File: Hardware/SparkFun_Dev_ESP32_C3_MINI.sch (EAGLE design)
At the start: 40 parts, among them J1 USB Female Type C Connector, J5 Vertical Qwiic Connector, U1 ESP32-C3_MINI-1, U2 RT9080-33GJ5

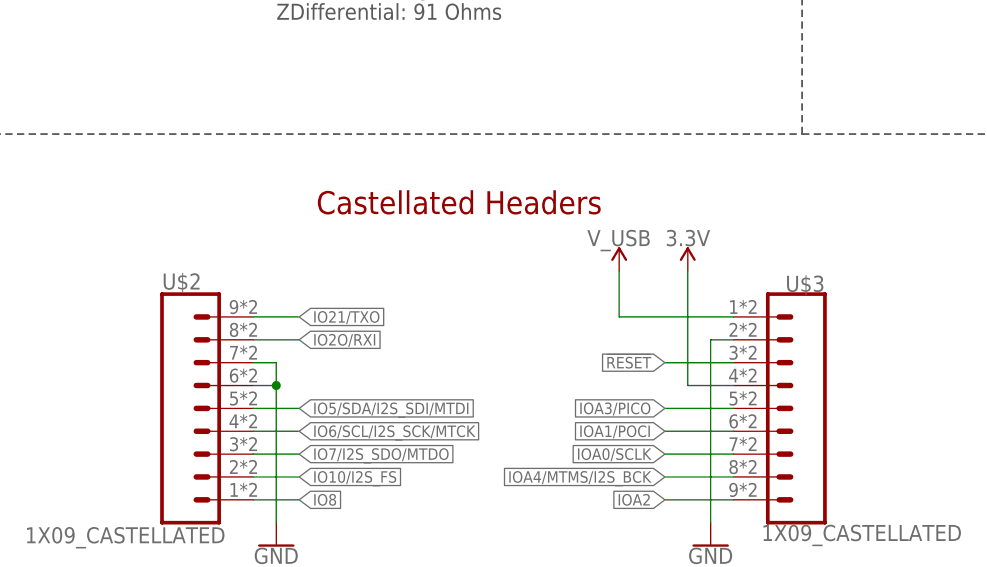
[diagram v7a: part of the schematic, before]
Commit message: Adds SparkFun logo
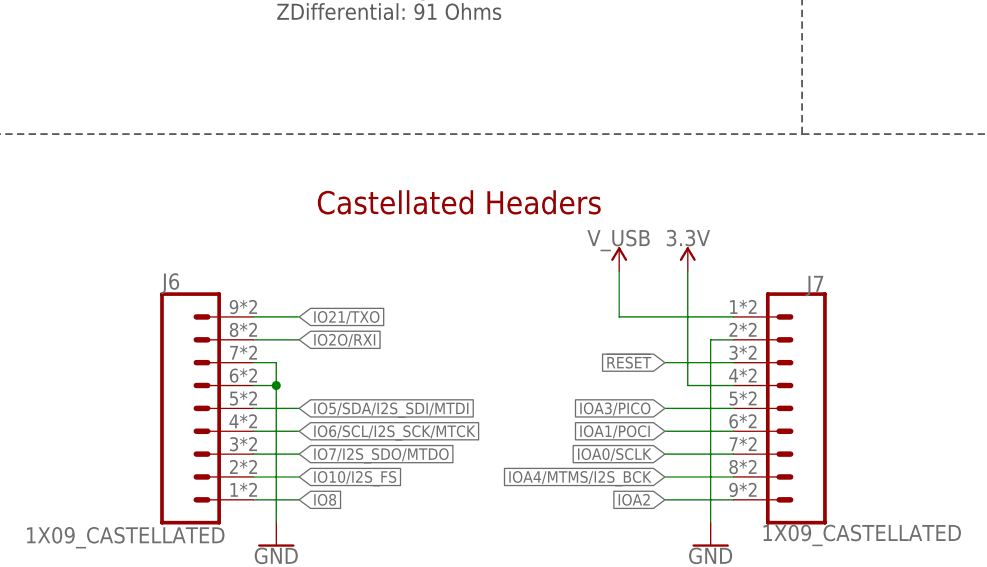
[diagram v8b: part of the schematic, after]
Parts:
- renumbered U$2 to J6, U$3 to J7
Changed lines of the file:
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@@
 <part name="GND1" library="SparkFun-PowerSymbols" deviceset="GND" device=""/>
 <part name="J5" library="SparkFun-Connectors" deviceset="QWIIC_CONNECTOR" device="" value="Vertical Qwiic Connector"/>
-<part name="U$2" library="ESP32-C3-MINI-1" deviceset="1X09_CASTELLATED" device=""/>
-<part name="U$3" library="ESP32-C3-MINI-1" deviceset="1X09_CASTELLATED" device=""/>
+<part name="J6" library="ESP32-C3-MINI-1" deviceset="1X09_CASTELLATED" device=""/>
+<part name="J7" library="ESP32-C3-MINI-1" deviceset="1X09_CASTELLATED" device=""/>
 <part name="SUPPLY5" library="SparkFun-PowerSymbols" deviceset="3.3V" device=""/>
 <part name="SUPPLY10" library="SparkFun-PowerSymbols" deviceset="V_USB" device=""/>
@@
 <attribute name="NAME" x="408.94" y="78.994" size="1.778" layer="95" font="vector"/>
 </instance>
-<instance part="U$2" gate="G$1" x="381" y="132.08" smashed="yes">
+<instance part="J6" gate="G$1" x="381" y="132.08" smashed="yes">
 <attribute name="VALUE" x="365.76" y="117.094" size="1.778" layer="96" font="vector"/>
 <attribute name="NAME" x="381" y="145.288" size="1.778" layer="95" font="vector"/>
 </instance>
-<instance part="U$3" gate="G$1" x="454.66" y="132.08" smashed="yes" rot="R180">
+<instance part="J7" gate="G$1" x="454.66" y="132.08" smashed="yes" rot="R180">
 <attribute name="VALUE" x="469.9" y="119.126" size="1.778" layer="96" font="vector" rot="R180"/>
 <attribute name="NAME" x="454.66" y="146.812" size="1.778" layer="95" font="vector" rot="R180"/>
@@
 <wire x1="439.42" y1="134.62" x2="439.42" y2="147.32" width="0.1524" layer="91"/>
 <pinref part="SUPPLY5" gate="G$1" pin="3.3V"/>
-<pinref part="U$3" gate="G$1" pin="4"/>
+<pinref part="J7" gate="G$1" pin="4"/>
 </segment>
 </net>
@@
 <junction x="393.7" y="134.62"/>
 <pinref part="GND16" gate="1" pin="GND"/>
-<pinref part="U$2" gate="G$1" pin="6"/>
-<pinref part="U$2" gate="G$1" pin="7"/>
+<pinref part="J6" gate="G$1" pin="6"/>
+<pinref part="J6" gate="G$1" pin="7"/>
 </segment>
 <segment>
@@
 <wire x1="441.96" y1="139.7" x2="441.96" y2="119.38" width="0.1524" layer="91"/>
 <pinref part="GND5" gate="1" pin="GND"/>
-<pinref part="U$3" gate="G$1" pin="2"/>
+<pinref part="J7" gate="G$1" pin="2"/>
 </segment>
 </net>
@@
 <wire x1="431.8" y1="142.24" x2="431.8" y2="147.32" width="0.1524" layer="91"/>
 <pinref part="SUPPLY10" gate="G$1" pin="V_USB"/>
-<pinref part="U$3" gate="G$1" pin="1"/>
+<pinref part="J7" gate="G$1" pin="1"/>
 </segment>
 </net>
@@
 <wire x1="444.5" y1="137.16" x2="436.88" y2="137.16" width="0.1524" layer="91"/>
 <label x="436.88" y="137.16" size="1.27" layer="95" font="vector" rot="R180" xref="yes"/>
-<pinref part="U$3" gate="G$1" pin="3"/>
+<pinref part="J7" gate="G$1" pin="3"/>
 </segment>
 </net>
@@
 <wire x1="396.24" y1="121.92" x2="391.16" y2="121.92" width="0.1524" layer="91"/>
 <label x="396.24" y="121.92" size="1.27" layer="95" font="vector" xref="yes"/>
-<pinref part="U$2" gate="G$1" pin="1"/>
+<pinref part="J6" gate="G$1" pin="1"/>
 </segment>
 </net>
@@
 <wire x1="391.16" y1="139.7" x2="396.24" y2="139.7" width="0.1524" layer="91"/>
 <label x="396.24" y="139.7" size="1.27" layer="95" font="vector" xref="yes"/>
-<pinref part="U$2" gate="G$1" pin="8"/>
+<pinref part="J6" gate="G$1" pin="8"/>
 </segment>
 <segment>
@@
 <wire x1="391.16" y1="142.24" x2="396.24" y2="142.24" width="0.1524" layer="91"/>
 <label x="396.24" y="142.24" size="1.27" layer="95" font="vector" xref="yes"/>
-<pinref part="U$2" gate="G$1" pin="9"/>
+<pinref part="J6" gate="G$1" pin="9"/>
 </segment>
 <segment>
@@
 <wire x1="436.88" y1="121.92" x2="444.5" y2="121.92" width="0.1524" layer="91"/>
 <label x="436.88" y="121.92" size="1.27" layer="95" font="vector" rot="R180" xref="yes"/>
-<pinref part="U$3" gate="G$1" pin="9"/>
+<pinref part="J7" gate="G$1" pin="9"/>
 </segment>
 </net>
@@
 <wire x1="436.88" y1="132.08" x2="444.5" y2="132.08" width="0.1524" layer="91"/>
 <label x="436.88" y="132.08" size="1.27" layer="95" font="vector" rot="R180" xref="yes"/>
-<pinref part="U$3" gate="G$1" pin="5"/>
+<pinref part="J7" gate="G$1" pin="5"/>
 </segment>
 </net>
@@
 <wire x1="436.88" y1="129.54" x2="444.5" y2="129.54" width="0.1524" layer="91"/>
 <label x="436.88" y="129.54" size="1.27" layer="95" font="vector" rot="R180" xref="yes"/>
-<pinref part="U$3" gate="G$1" pin="6"/>
+<pinref part="J7" gate="G$1" pin="6"/>
 </segment>
 </net>
@@
 <wire x1="396.24" y1="124.46" x2="391.16" y2="124.46" width="0.1524" layer="91"/>
 <label x="396.24" y="124.46" size="1.27" layer="95" font="vector" xref="yes"/>
-<pinref part="U$2" gate="G$1" pin="2"/>
+<pinref part="J6" gate="G$1" pin="2"/>
 </segment>
 <segment>
@@
 <wire x1="436.88" y1="124.46" x2="444.5" y2="124.46" width="0.1524" layer="91"/>
 <label x="436.88" y="124.46" size="1.27" layer="95" font="vector" rot="R180" xref="yes"/>
-<pinref part="U$3" gate="G$1" pin="8"/>
+<pinref part="J7" gate="G$1" pin="8"/>
 </segment>
 <segment>
@@
 <wire x1="396.24" y1="132.08" x2="391.16" y2="132.08" width="0.1524" layer="91"/>
 <label x="396.24" y="132.08" size="1.27" layer="95" font="vector" xref="yes"/>
-<pinref part="U$2" gate="G$1" pin="5"/>
+<pinref part="J6" gate="G$1" pin="5"/>
 </segment>
 <segment>
@@
 <wire x1="396.24" y1="129.54" x2="391.16" y2="129.54" width="0.1524" layer="91"/>
 <label x="396.24" y="129.54" size="1.27" layer="95" font="vector" rot="MR180" xref="yes"/>
-<pinref part="U$2" gate="G$1" pin="4"/>
+<pinref part="J6" gate="G$1" pin="4"/>
 </segment>
 <segment>
@@
 <wire x1="396.24" y1="127" x2="391.16" y2="127" width="0.1524" layer="91"/>
 <label x="396.24" y="127" size="1.27" layer="95" font="vector" rot="MR180" xref="yes"/>
-<pinref part="U$2" gate="G$1" pin="3"/>
+<pinref part="J6" gate="G$1" pin="3"/>
 </segment>
 <segment>
@@
 <wire x1="436.88" y1="127" x2="444.5" y2="127" width="0.1524" layer="91"/>
 <label x="436.88" y="127" size="1.27" layer="95" font="vector" rot="R180" xref="yes"/>
-<pinref part="U$3" gate="G$1" pin="7"/>
-</segment>
-<segment>
+<pinref part="J7" gate="G$1" pin="7"/>
+</segment>
+<segment>
